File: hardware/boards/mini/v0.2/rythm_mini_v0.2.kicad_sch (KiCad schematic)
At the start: 102 parts, among them IC1 NAU88C22YG, IC3 IS42S16160J-6BLI, J2 Top, J3 Bottom, Q1 PMV37EN22, U1 W25Q128JVP, U2 LTV-217-G, U4 STM32H750XBHx, Y1 Crystal_GND24

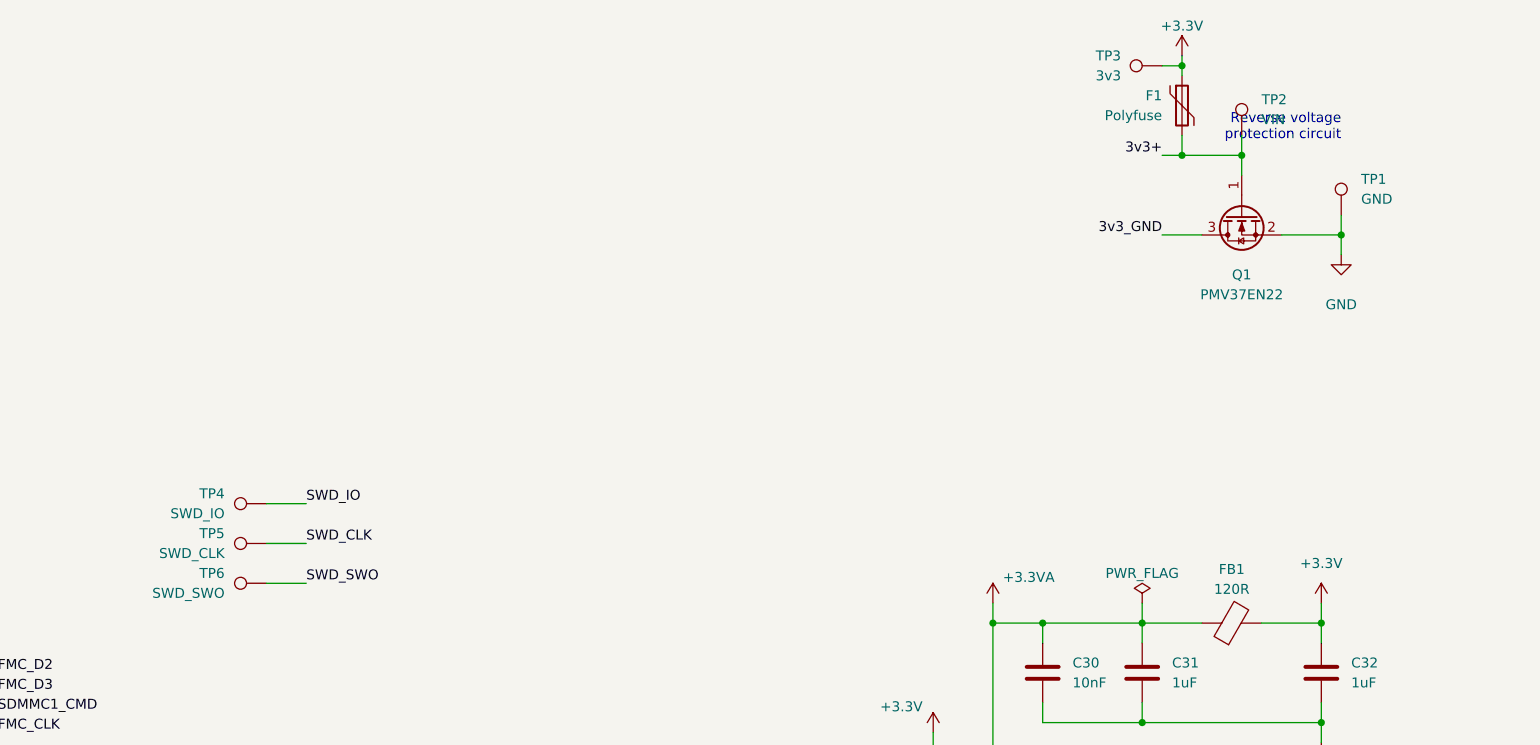
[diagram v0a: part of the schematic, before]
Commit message: mini: remove unused test points
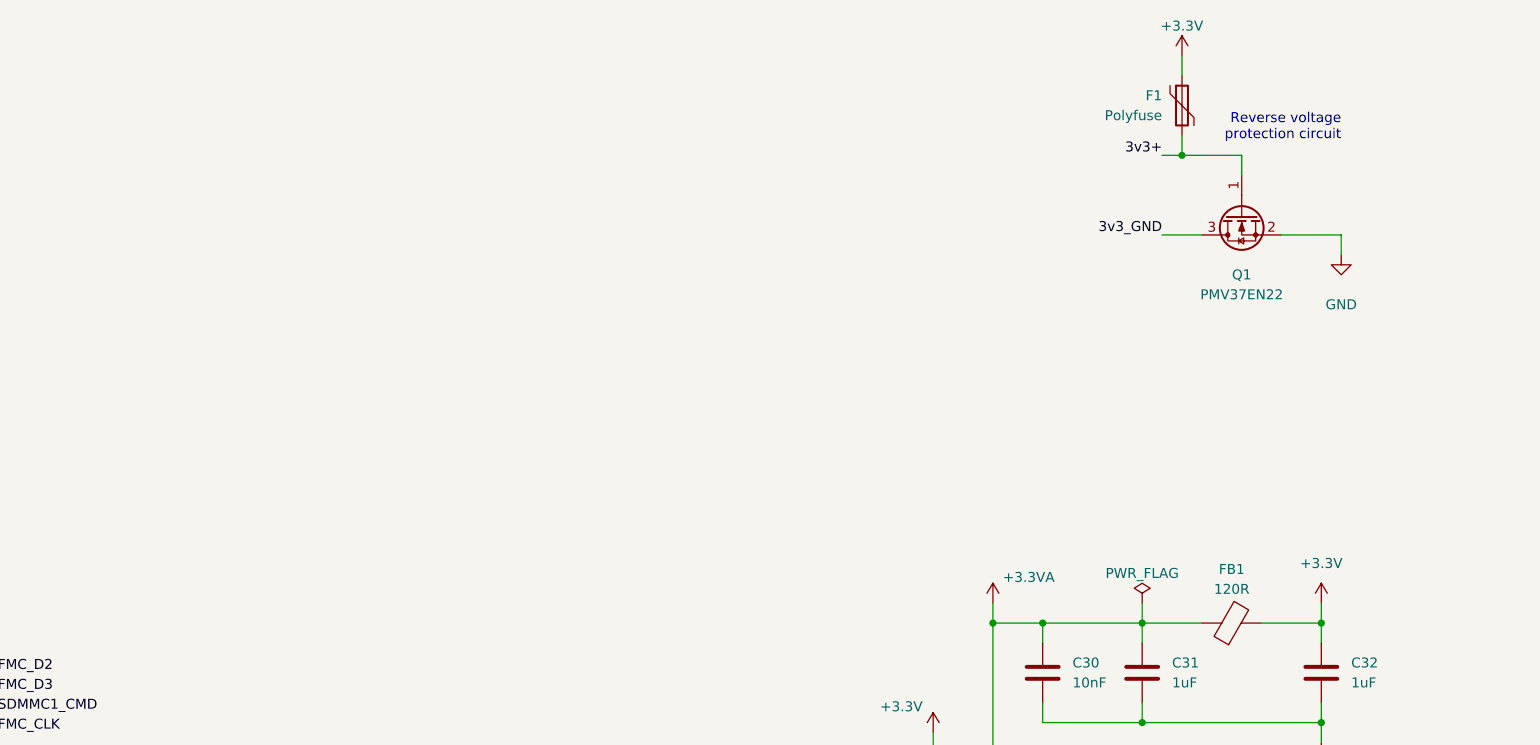
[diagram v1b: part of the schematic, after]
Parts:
- removed TP1: GND, TestPoint:TestPoint_Pad_D1.0mm, symbol Connector:TestPoint
- removed TP2: VIN, TestPoint:TestPoint_Pad_D1.0mm, symbol Connector:TestPoint
- removed TP3: 3v3, TestPoint:TestPoint_Pad_D1.0mm, symbol Connector:TestPoint
- removed TP4: SWD_IO, TestPoint:TestPoint_Pad_D1.0mm, symbol Connector:TestPoint
- removed TP5: SWD_CLK, TestPoint:TestPoint_Pad_D1.0mm, symbol Connector:TestPoint
- removed TP6: SWD_SWO, TestPoint:TestPoint_Pad_D1.0mm, symbol Connector:TestPoint

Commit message: mini: start routing QSPI to lower connector
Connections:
- net QSPI_CS_EXP: now reaches U4.G15 (PG6)
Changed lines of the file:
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@@
 	(wire
 		(pts
+			(xy 10.16 227.33) (xy 12.7 227.33)
+		)
+		(stroke
+			(width 0)
+			(type default)
+		)
+	)
+	(wire
+		(pts
 			(xy 237.49 33.02) (xy 250.19 33.02)
 		)
@@
 		)
 	)
+	(label "QSPI_CS_EXP"
+		(at 12.7 227.33 0)
+		(effects
+			(font
+				(size 1.27 1.27)
+			)
+			(justify left bottom)
+		)
+	)
 	(label "SPKR"
 		(at 394.97 149.86 0)
@@
 		)
 	)
+	(label "QSPI_IO2"
+		(at 471.17 147.32 180)
+		(effects
+			(font
+				(size 1.27 1.27)
+			)
+			(justify right bottom)
+		)
+	)
 	(label "FMC_D4"
 		(at 104.14 113.03 0)
@@
 		)
 	)
+	(label "QSPI_IO0"
+		(at 471.17 142.24 180)
+		(effects
+			(font
+				(size 1.27 1.27)
+			)
+			(justify right bottom)
+		)
+	)
 	(label "PA8"
 		(at 53.34 64.77 0)
@@
 		)
 	)
+	(label "QSPI_IO1"
+		(at 471.17 144.78 180)
+		(effects
+			(font
+				(size 1.27 1.27)
+			)
+			(justify right bottom)
+		)
+	)
 	(label "PH7"
 		(at 12.7 278.13 0)
@@
 		)
 	)
+	(label "QSPI_CLK"
+		(at 471.17 139.7 180)
+		(effects
+			(font
+				(size 1.27 1.27)
+			)
+			(justify right bottom)
+		)
+	)
 	(label "SAI1_FS"
 		(at 104.14 105.41 0)
@@
 		)
 	)
+	(label "QSPI_CS_EXP"
+		(at 463.55 135.89 0)
+		(effects
+			(font
+				(size 1.27 1.27)
+			)
+			(justify left bottom)
+		)
+	)
 	(label "SPKL"
 		(at 394.97 144.78 0)
@@
 		)
 	)
+	(label "QSPI_IO3"
+		(at 471.17 149.86 180)
+		(effects
+			(font
+				(size 1.27 1.27)
+			)
+			(justify right bottom)
+		)
+	)

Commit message: mini: route external QSPI lines and LEDs
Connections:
- net DIN_OUT_SINK: now also J3.27; no longer J3.25
- net DIN_OUT_SOURCE: now also J3.25; no longer J3.27
- net LED_STATUS: now also U4.E3 (PC13); no longer U4.F14 (PC6)
- net LED_STATUS2: now also U4.E2 (PI9)
- net QSPI_CLK: now also J3.54
- net QSPI_CS_EXP: now also J3.44
- net QSPI_IO0: now also J3.52
- net QSPI_IO1: now also J3.50
- net QSPI_IO2: now also J3.48
- net QSPI_IO3: now also J3.46
- net EXT_QSPI_DETECT: now reaches U4.H15 (PG3)
- net EXT_QSPI_DETECT: now also J3.42
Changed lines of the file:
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@@
 	(wire
 		(pts
+			(xy 547.37 95.25) (xy 552.45 95.25)
+		)
+		(stroke
+			(width 0)
+			(type default)
+		)
+	)
+	(wire
+		(pts
 			(xy 189.23 78.74) (xy 189.23 76.2)
 		)
@@
 	(wire
 		(pts
+			(xy 547.37 102.87) (xy 552.45 102.87)
+		)
+		(stroke
+			(width 0)
+			(type default)
+		)
+	)
+	(wire
+		(pts
 			(xy 267.97 87.63) (xy 271.78 87.63)
 		)
@@
 	(wire
 		(pts
-			(xy 50.8 163.83) (xy 53.34 163.83)
-		)
-		(stroke
-			(width 0)
-			(type default)
-		)
-	)
-	(wire
-		(pts
 			(xy 386.08 273.05) (xy 388.62 273.05)
 		)
@@
 	(wire
 		(pts
+			(xy 547.37 90.17) (xy 552.45 90.17)
+		)
+		(stroke
+			(width 0)
+			(type default)
+		)
+	)
+	(wire
+		(pts
 			(xy 482.6 44.45) (xy 487.68 44.45)
 		)
@@
 	(wire
 		(pts
+			(xy 547.37 105.41) (xy 552.45 105.41)
+		)
+		(stroke
+			(width 0)
+			(type default)
+		)
+	)
+	(wire
+		(pts
 			(xy 196.85 58.42) (xy 196.85 64.77)
 		)
@@
 	(wire
 		(pts
+			(xy 547.37 97.79) (xy 552.45 97.79)
+		)
+		(stroke
+			(width 0)
+			(type default)
+		)
+	)
+	(wire
+		(pts
 			(xy 50.8 115.57) (xy 53.34 115.57)
 		)
@@
 	(wire
 		(pts
+			(xy 10.16 332.74) (xy 15.24 332.74)
+		)
+		(stroke
+			(width 0)
+			(type default)
+		)
+	)
+	(wire
+		(pts
 			(xy 396.24 261.62) (xy 398.78 261.62)
 		)
@@
 	(wire
 		(pts
+			(xy 50.8 181.61) (xy 53.34 181.61)
+		)
+		(stroke
+			(width 0)
+			(type default)
+		)
+	)
+	(wire
+		(pts
 			(xy 265.43 33.02) (xy 273.05 33.02)
 		)
@@
 	(wire
 		(pts
+			(xy 547.37 92.71) (xy 552.45 92.71)
+		)
+		(stroke
+			(width 0)
+			(type default)
+		)
+	)
+	(wire
+		(pts
+			(xy 547.37 100.33) (xy 552.45 100.33)
+		)
+		(stroke
+			(width 0)
+			(type default)
+		)
+	)
+	(wire
+		(pts
 			(xy 482.6 87.63) (xy 487.68 87.63)
 		)
@@
 	(wire
 		(pts
+			(xy 10.16 219.71) (xy 12.7 219.71)
+		)
+		(stroke
+			(width 0)
+			(type default)
+		)
+	)
+	(wire
+		(pts
 			(xy 12.7 217.17) (xy 10.16 217.17)
 		)
@@
 	)
 	(label "QSPI_IO2"
-		(at 471.17 147.32 180)
+		(at 552.45 97.79 0)
 		(effects
 			(font
 				(size 1.27 1.27)
 			)
-			(justify right bottom)
+			(justify left bottom)
 		)
 	)
@@
 	)
 	(label "LED_STATUS"
-		(at 53.34 163.83 0)
+		(at 53.34 181.61 0)
 		(effects
 			(font
@@
 		)
 	)
+	(label "EXT_QSPI_DETECT"
+		(at 12.7 219.71 0)
+		(effects
+			(font
+				(size 1.27 1.27)
+			)
+			(justify left bottom)
+		)
+	)
 	(label "FMC_D7"
 		(at 154.94 255.27 0)
@@
 	)
 	(label "QSPI_IO0"
-		(at 471.17 142.24 180)
+		(at 552.45 102.87 0)
 		(effects
 			(font
 				(size 1.27 1.27)
 			)
-			(justify right bottom)
+			(justify left bottom)
 		)
 	)
@@
 	)
 	(label "QSPI_IO1"
-		(at 471.17 144.78 180)
+		(at 552.45 100.33 0)
 		(effects
 			(font
 				(size 1.27 1.27)
 			)
-			(justify right bottom)
+			(justify left bottom)
 		)
 	)
@@
 	)
 	(label "QSPI_CLK"
-		(at 471.17 139.7 180)
+		(at 552.45 105.41 0)
 		(effects
 			(font
 				(size 1.27 1.27)
 			)
-			(justify right bottom)
+			(justify left bottom)
 		)
 	)
@@
 	)
 	(label "DIN_OUT_SOURCE"
-		(at 519.43 72.39 180)
+		(at 519.43 69.85 180)
 		(effects
 			(font
@@
 		)
 	)
+	(label "LED_STATUS2"
+		(at 15.24 332.74 0)
+		(effects
+			(font
+				(size 1.27 1.27)
+			)
+			(justify left bottom)
+		)
+	)
 	(label "PA12{slash}4TX"
 		(at 53.34 74.93 0)
@@
 	)
 	(label "DIN_OUT_SINK"
-		(at 519.43 69.85 180)
+		(at 519.43 72.39 180)
 		(effects
 			(font
@@
 		)
 	)
+	(label "EXT_QSPI_DETECT"
+		(at 552.45 90.17 0)
+		(effects
+			(font
+				(size 1.27 1.27)
+			)
+			(justify left bottom)
+		)
+	)
 	(label "SWD_SWO"
 		(at 53.34 102.87 0)
@@
 	)
 	(label "QSPI_CS_EXP"
-		(at 463.55 135.89 0)
+		(at 552.45 92.71 0)
 		(effects
 			(font
@@
 	)
 	(label "QSPI_IO3"
-		(at 471.17 149.86 180)
+		(at 552.45 95.25 0)
 		(effects
 			(font
 				(size 1.27 1.27)
 			)
-			(justify right bottom)
+			(justify left bottom)
 		)
 	)
